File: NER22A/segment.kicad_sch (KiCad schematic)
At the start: 201 parts

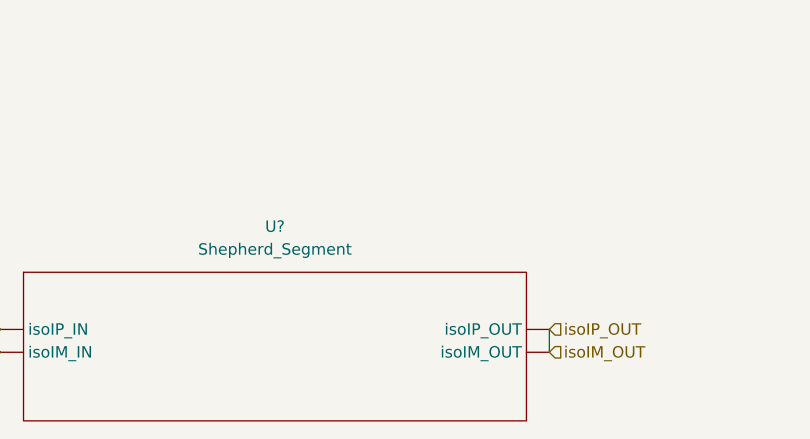
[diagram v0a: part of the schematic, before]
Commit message: Added LV Circuits
Added a first pass of all LV circuits to the Master Schematic. Also moved HV stuff into sub-sheets
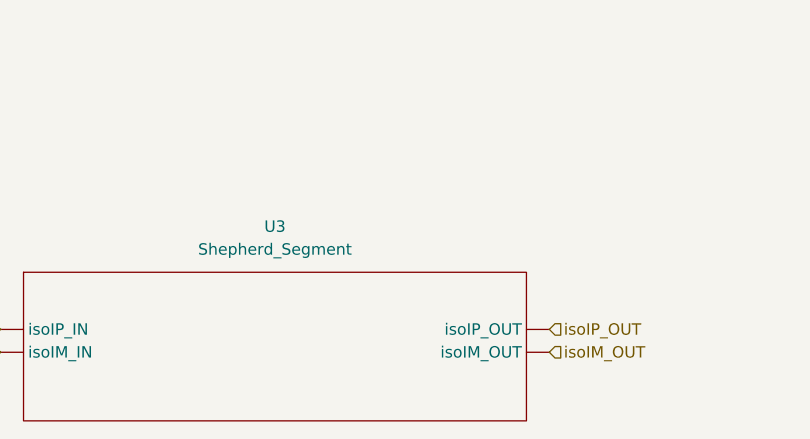
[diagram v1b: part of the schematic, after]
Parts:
- gave numbers to parts that had none: 201
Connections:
- new net isoIP_OUT: U3. (isoIP_OUT)
